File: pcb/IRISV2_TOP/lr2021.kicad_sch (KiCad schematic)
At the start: 50 parts, among them J7 Conn_Coaxial, J8 Conn_Coaxial, U9 lr2021, Y5 ECS-TXO-32CSMV-320-AN-TR

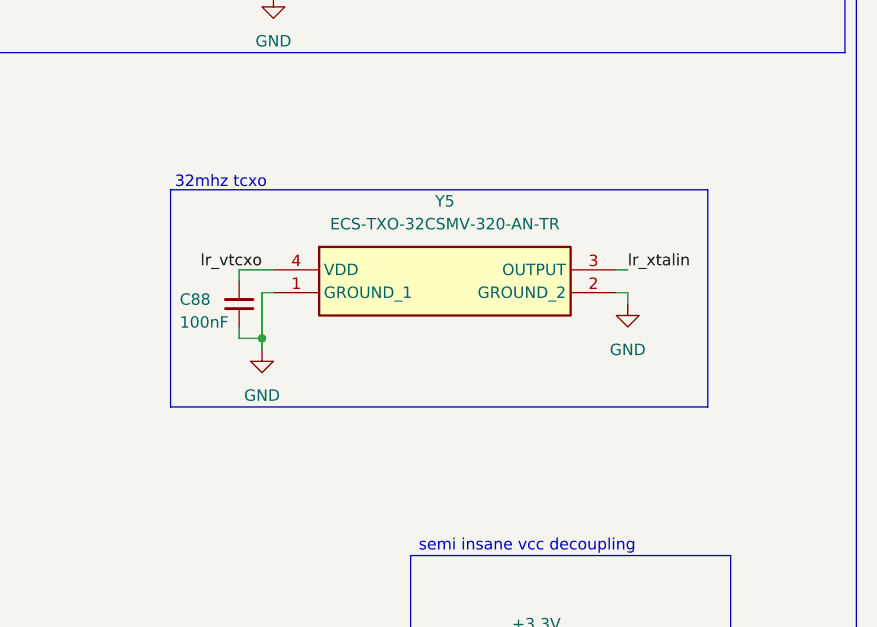
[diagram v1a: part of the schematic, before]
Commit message: fixed some issues, lr2021 matching is now 0201 - todo change trace width to match pad width like ref design, see todo for rest
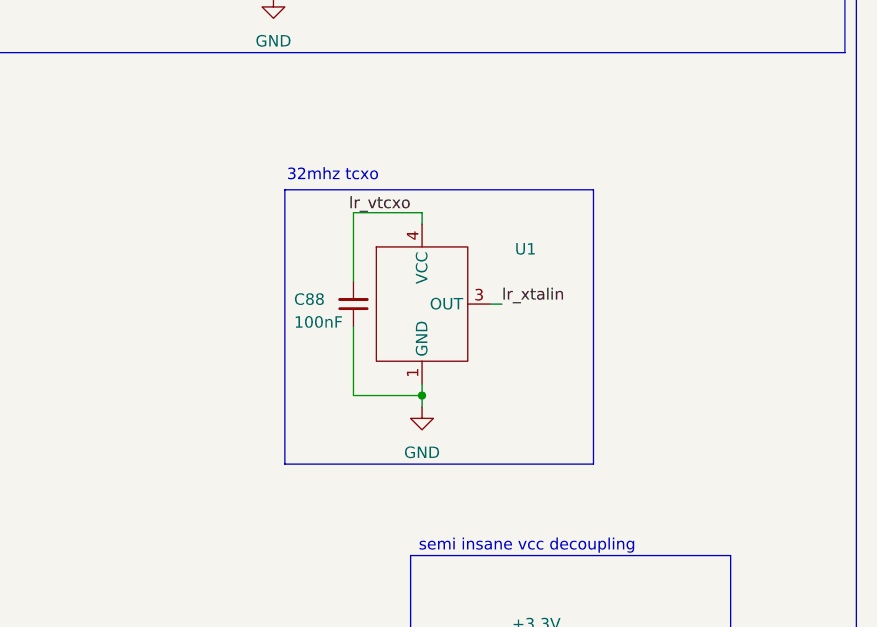
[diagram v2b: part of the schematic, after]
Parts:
- removed Y5: ECS-TXO-32CSMV-320-AN-TR, ECS-TXO-32CSMV-320-AN:ECSTXO32CSMV320ANTR, symbol ECS-TXO-32CSMV-320-AN-TR:ECS-TXO-32CSMV-320-AN-TR
- added U1: ~, ECS-TXO-20CSMV4:ECS-TXO-20CSMV4, symbol ECS-TXO-20CSMV4:ECS-TXO-20CSMV4
- C71, C75, C76, C77, C78, C79, C82, C84, C86, C87, C89, C90, C91, C92: footprint Capacitor_SMD:C_0402_1005Metric -> Capacitor_SMD:C_0201_0603Metric
- L10, L11, L12, L13, L14, L15, L4, L5, L6, L7, L9: footprint Inductor_SMD:L_0402_1005Metric -> Inductor_SMD:L_0201_0603Metric
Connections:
- net GND: now also U1.1 (GND)
- net lr_vtcxo: now also U1.4 (VCC)
- net lr_xtalin: now also U1.3 (OUT)
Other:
- moved on the sheet: C88
